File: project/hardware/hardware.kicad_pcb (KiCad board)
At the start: 4 copper layers, 102 parts, among them IC1 TAS5760LDAPR, J1 798-DM3D-SF, J2 Conn_01x04, J3 Conn_01x04, J4 USB-C, SW1 SW_Push, SW2 SW_Push, SW3 SW_Push, SW5 SW_Push, U1 TPS563200, U2 ESP32-S3, U3 USBLC6-2SC6, Y1 ECS-400-10-36B2-CKM-TR, Y2 ABS07-166-32.768KHZ-T

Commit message: finally changed the 'planes'
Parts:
- moved R16 89.9 mm to (173.7, 88.8)
- moved R20 89.9 mm to (173.7, 90.6)
- moved SW1 89.9 mm to (167.6, 88.7)
- moved SW2 89.9 mm to (167.6, 93.4)
- moved C28 89.9 mm to (173.5, 94.1)
- moved C34 89.9 mm to (173.5, 96.0)
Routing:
- net 3V3: track 44.4 -> 47.6 mm
- net Net-(C14-Pad1): track 3.27 -> 2.68 mm
- added copper zone on F.Cu, net 12
- added copper zone on F.Cu, net 3V3
- added copper zone on F.Cu, net Net-(C9-Pad2)
- added copper zone on F.Cu, net Net-(IC1-SPK_OUTA+)
- added copper zone on F.Cu, net Net-(IC1-SPK_OUTB+)
- added copper zone on F.Cu, net Net-(JP3-A)
- added copper zone on F.Cu, net Net-(JP3-B)
- added copper zone on F.Cu, net Net-(JP4-A)
- added copper zone on F.Cu, net Net-(JP4-B)

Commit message: alimentação
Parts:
- moved C17 8.87 mm to (152.8, 62.7), turned to 180 degrees
- moved L4 8.65 mm to (147.2, 64.8), turned to 90 degrees
- moved C20 4.96 mm to (152.8, 61.0), turned to 180 degrees
- moved C21 2.24 mm to (152.8, 59.4), turned to 180 degrees
- moved C15 1.02 mm to (167.1, 61.6)
- moved C11 0.73 mm to (160.0, 65.2)
- moved C6 0.66 mm to (155.5, 65.2)
- moved C8 0.66 mm to (158.0, 65.2)
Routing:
- net 3V3: track 47.6 -> 73.7 mm, vias 7 -> 8
- net 12: track 13.7 -> 9.97 mm
- net Net-(U1-VBST): track 3.85 -> 4.74 mm
- net Net-(U1-SW): track 11.6 -> 11.0 mm
- net Net-(JP4-A): vias 0 -> 4
- net Net-(JP4-B): vias 0 -> 1
- net GPIO_45_46: vias 61 -> 70
- added copper zone on F.Cu, net Net-(U1-SW)
- added copper zone on F.Cu, net PWR_GND

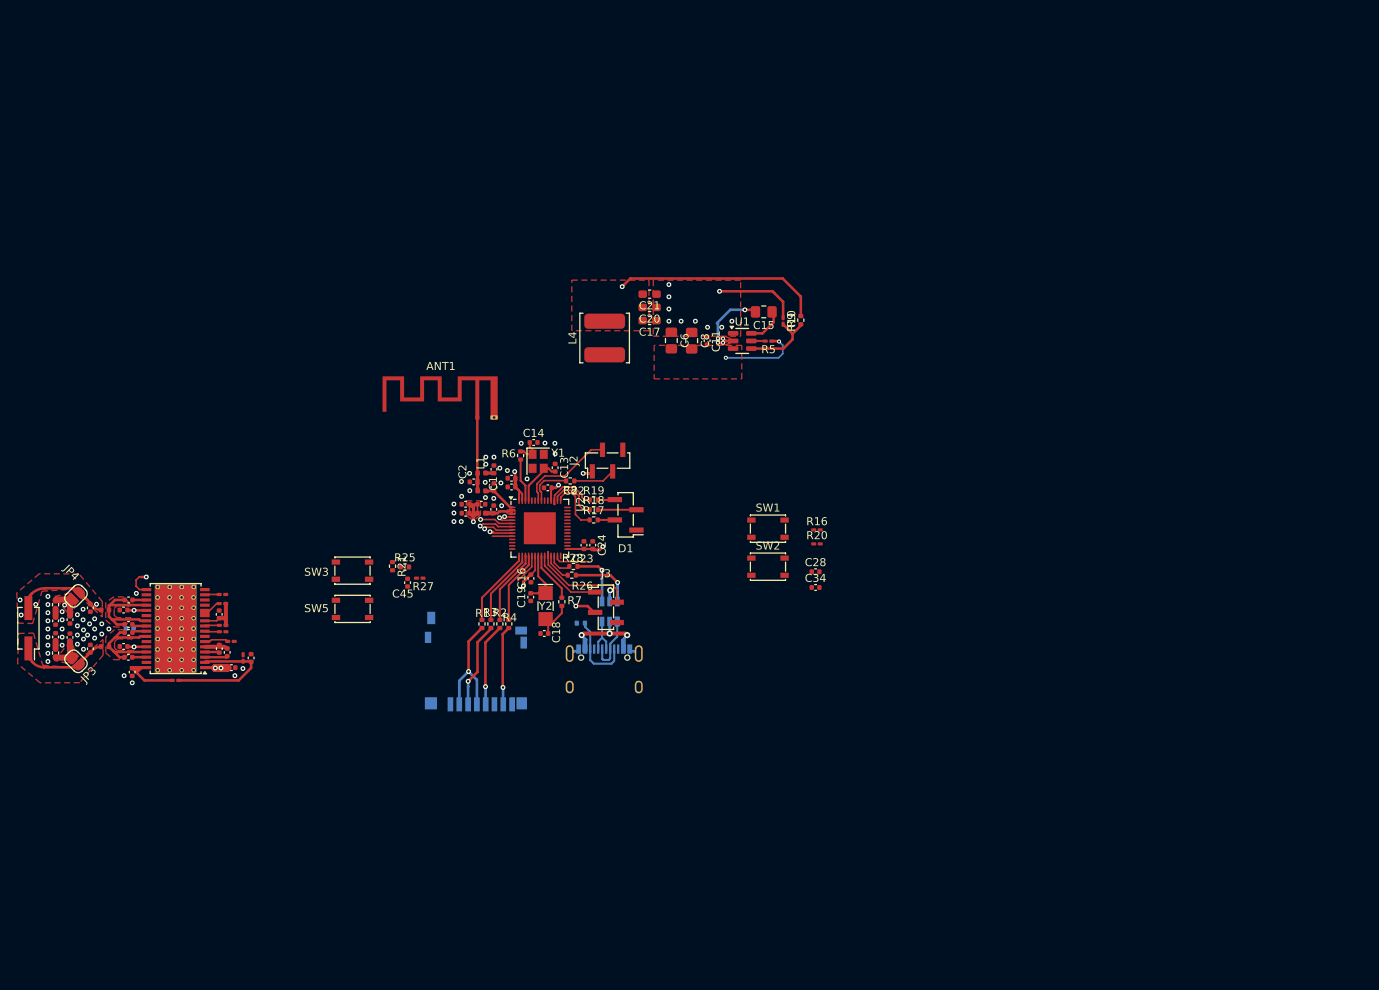
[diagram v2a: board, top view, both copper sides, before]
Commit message: faltando o plano de terra da antena
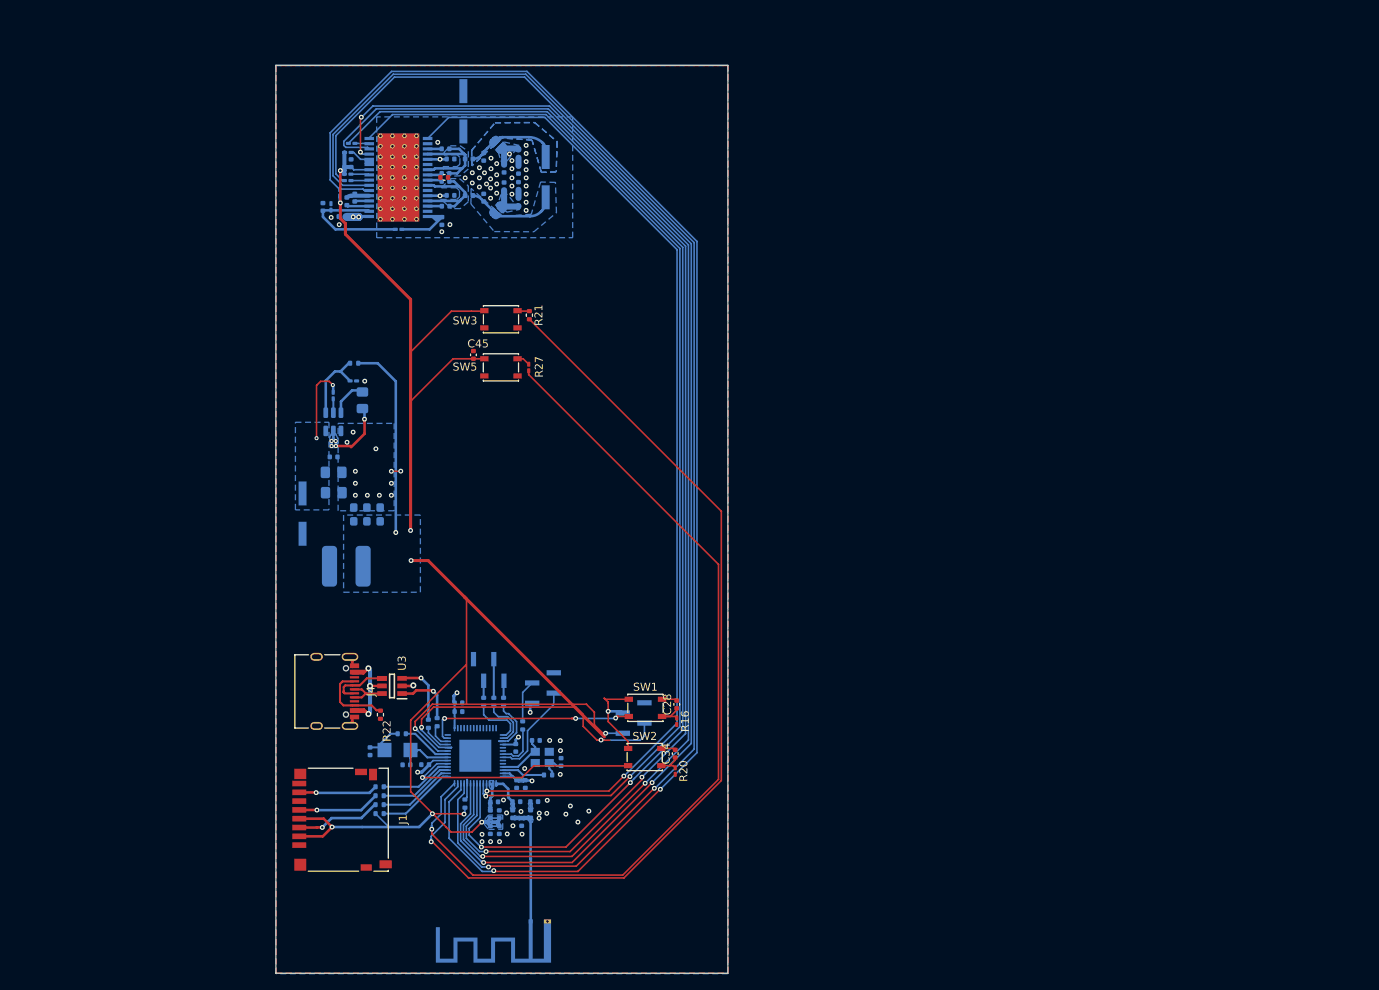
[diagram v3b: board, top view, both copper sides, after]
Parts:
- added J5: Conn_01x02_Socket, Connector_PinSocket_2.54mm:PinSocket_2x01_P2.54mm_Vertical_SMD, B.Cu at (109.4, 86.8)
- added J6: Conn_01x02_Socket, Connector_PinSocket_2.54mm:PinSocket_2x01_P2.54mm_Vertical_SMD, B.Cu at (129.5, 36.5)
- ?, C38, J1, J4, R22, U3: moved to F.Cu
- ANT1, C1, C10, C11, C12, C13, C14, C15, C16, C17, C18, C19, C2, C20, C21, C22, C23, C24, C25, C26, C27, C29, C3, C30, C31, C32, C33, C35, C36, C37, C39, C4, C40, C41, C42, C43, C44, C46, C5, C6, C7, C8, C9, D1, IC1, J2, J3, JP3, JP4, L1, L2, L3, L4, L5, L6, LS1, R1, R10, R11, R12, R13, R14, R15, R17, R18, R19, R2, R23, R24, R25, R26, R28, R29, R3, R30, R4, R5, R6, R7, R8, R9, U1, U2, Y1, Y2: moved to B.Cu
- moved LS1 85.8 mm to (139.8, 44.7)
- moved C43 80.8 mm to (136.4, 45.8)
- moved C44 80.8 mm to (136.4, 43.8)
- moved R23 80.8 mm to (136.4, 47.8)
- moved R24 80.8 mm to (136.4, 41.8)
- moved C40 78.3 mm to (134.6, 45.9)
- moved C41 78.3 mm to (134.6, 43.7)
- moved JP3 77.2 mm to (133.8, 48.9), turned to -135 degrees
- moved JP4 77.2 mm to (133.8, 40.7), turned to -45 degrees
- moved C35 74.8 mm to (132.0, 47.3)
- moved C36 74.8 mm to (132.0, 42.2)
- moved L6 72.4 mm to (130.2, 42.5), turned to 0 degrees
- moved L5 72.4 mm to (130.2, 47.0), turned to 0 degrees
- moved C39 69.6 mm to (127.9, 42.5), turned to 180 degrees
- moved C37 69.6 mm to (127.9, 47.0), turned to 180 degrees
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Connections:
- C11 pad 1: PWR_GND -> GPIO_45_46
- C13 pad 1: GPIO_45_46 -> GND
- C14 pad 2: GPIO_45_46 -> GND
- C17 pad 1: PWR_GND -> GPIO_45_46
- C18 pad 2: GPIO_45_46 -> GND
- C19 pad 1: GPIO_45_46 -> GND
- C20 pad 1: PWR_GND -> GPIO_45_46
- C21 pad 1: PWR_GND -> GPIO_45_46
- C25 pad 2: GPIO_45_46 -> GND
- C30 pad 1: GPIO_45_46 -> GND_ANALOG
- C35 pad 1: GPIO_45_46 -> GND_ANALOG
- C36 pad 2: GPIO_45_46 -> GND_ANALOG
- C37 pad 1: GPIO_45_46 -> GND_ANALOG
- C38 pad 1: GPIO_45_46 -> GND_ANALOG
- C39 pad 1: GPIO_45_46 -> GND_ANALOG
- C40 pad 1: GPIO_45_46 -> GND_ANALOG
- C41 pad 2: GPIO_45_46 -> GND_ANALOG
- C42 pad 1: GPIO_45_46 -> GND_ANALOG
- C43 pad 1: GPIO_45_46 -> GND_ANALOG
- C44 pad 2: GPIO_45_46 -> GND_ANALOG
- C46 pad 2: GPIO_45_46 -> GND
- C6 pad 1: PWR_GND -> GPIO_45_46
- C8 pad 1: PWR_GND -> GPIO_45_46
- IC1 pad 18: GPIO_45_46 -> GND_ANALOG
- IC1 pad 22: GPIO_45_46 -> GND_ANALOG
- IC1 pad 27: GPIO_45_46 -> GND_ANALOG
- IC1 pad 31: GPIO_45_46 -> GND_ANALOG
- IC1 pad 33: GPIO_45_46 -> GND_ANALOG
- J4 pad A1: GPIO_45_46 -> GND
- J4 pad A12: GPIO_45_46 -> GND
- J4 pad B1: GPIO_45_46 -> GND
- J4 pad B12: GPIO_45_46 -> GND
- J4 pad S1: GPIO_45_46 -> GND
- R22 pad 2: GPIO_45_46 -> GND
- R29 pad 2: GPIO_45_46 -> GND
- U1 pad 1: PWR_GND -> GPIO_45_46
- U2 pad 19: BT_L -> BT_R
- U2 pad 27: BT_R -> BT_L
- U3 pad 2: GPIO_45_46 -> GND
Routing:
- net 3V3: track 73.7 -> 261.7 mm, vias 8 -> 14
- net AUDIO_FAULT: track 3.03 -> 179.5 mm, vias 0 -> 2
- net AUDIO_EN: track 0.00 -> 175.1 mm, vias 0 -> 2
- net I2C_DATA_IN: track 3.28 -> 168.8 mm, vias 1 -> 2
- net AUDIO_MUTE: track 3.73 -> 158.7 mm, vias 1 -> 4
- net AUDIO_CLK: track 4.34 -> 158.1 mm, vias 1 -> 2
- net I2C_CLK: track 4.48 -> 151.2 mm, vias 1 -> 2
- net SDIN: track 1.66 -> 136.3 mm, vias 1 -> 2
- net LRCK: track 4.97 -> 126.7 mm
- net BOOT: track 0.00 -> 119.8 mm, vias 0 -> 1
- net EN: track 0.01 -> 111.7 mm, vias 0 -> 1
- net BT_R: track 4.37 -> 33.9 mm, vias 0 -> 1
- net Display_SCL: track 13.6 -> 40.7 mm, vias 0 -> 2
- net Display_SDA: track 8.76 -> 35.6 mm, vias 0 -> 2
- net BT_L: track 3.83 -> 30.2 mm, vias 0 -> 3
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- added copper zone on B.Cu, net 12
- added copper zone on B.Cu, net 3V3
- added copper zone on B.Cu, net GND_ANALOG
- added copper zone on B.Cu, net GPIO_45_46
- added copper zone on F.Cu, net GPIO_45_46
- added copper zone on B.Cu, net Net-(ANT1-Pad1)
- added copper zone on B.Cu, net Net-(C1-Pad2)
- added copper zone on B.Cu, net Net-(C9-Pad2)
- added copper zone on B.Cu, net Net-(IC1-SPK_OUTA+)
- added copper zone on B.Cu, net Net-(IC1-SPK_OUTB+)
- added copper zone on B.Cu, net Net-(JP3-A)
- added copper zone on B.Cu, net Net-(JP3-B)
- added copper zone on B.Cu, net Net-(JP4-A)
- added copper zone on B.Cu, net Net-(JP4-B)
- added copper zone on B.Cu, net Net-(U1-SW)
- added copper zone on B.Cu, net Net-(U2-LNA_IN)
- removed copper zone on F.Cu, net 12
- removed copper zone on F.Cu, net 3V3
- removed copper zone on F.Cu, net Net-(C9-Pad2)
- removed copper zone on F.Cu, net Net-(IC1-SPK_OUTA+)
- removed copper zone on F.Cu, net Net-(IC1-SPK_OUTB+)
- removed copper zone on F.Cu, net Net-(JP3-A)
- removed copper zone on F.Cu, net Net-(JP3-B)
- removed copper zone on F.Cu, net Net-(JP4-A)
- removed copper zone on F.Cu, net Net-(JP4-B)
- removed copper zone on F.Cu, net Net-(U1-SW)
- removed copper zone on F.Cu, net PWR_GND
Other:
- board outline added: 56.5 x 113.5 mm

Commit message: plots
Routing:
- added copper zone on F.Cu, net 12
- added copper zone on F.Cu, net 3V3
- added copper zone on F.Cu, net GND_ANALOG
- added copper zone on F.Cu, net Net-(IC1-SPK_OUTA+)
- added copper zone on F.Cu, net Net-(IC1-SPK_OUTB+)
- added copper zone on F.Cu, net Net-(JP3-A)
- added copper zone on F.Cu, net Net-(JP3-B)
- added copper zone on F.Cu, net Net-(JP4-A)
- added copper zone on F.Cu, net Net-(JP4-B)
